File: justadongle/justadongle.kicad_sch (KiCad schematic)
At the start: 26 parts, among them U1 SL2.1A_C6798314, U2 FSUSB42MUX, U3 LMV7219M5X/NOPB, U4 HC-USB3.0-C26

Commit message: Added the footprints for all the componenets in the schematic
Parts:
- C1, C2, C3, C4, C5, C6, C7, C8, C9: footprint (none) -> Footprints:CAP-TH_BD5.0-P2.00-D0.8-FD
- D1, D2, D3, D4, D5: footprint (none) -> Footprints:SOD-323_L1.8-W1.3-LS2.5-RD
- R1, R2, R3: footprint (none) -> Footprints:RES-TH_BD2.4-L6.3-P10.30-D0.6
- U1: footprint (none) -> Footprints:SOP-16_L10.0-W3.9-P1.27-LS6.0-BL
- U2: footprint (none) -> Footprints:MSOP-10_L3.0-W3.0-P0.50-LS5.0-BL
- U3: footprint (none) -> Footprints:SOT-23-5_L3.0-W1.7-P0.95-LS2.8-BR
- U4: footprint (none) -> Footprints:USB-3.0-A-SMD_HC-USB3.0-C26
- USB2, USB3, USB4, USB5: footprint (none) -> Footprints:USB-A-TH_USB-231-ARY
- USB6: footprint (none) -> Footprints:USB-C-SMD_TYPE-C-6PIN-2MD-073
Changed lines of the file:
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@@
 			)
 		)
-		(property "Footprint" ""
+		(property "Footprint" "Footprints:SOD-323_L1.8-W1.3-LS2.5-RD"
 			(at 314.96 50.8 0)
 			(effects
@@
 			)
 		)
-		(property "Footprint" ""
+		(property "Footprint" "Footprints:USB-A-TH_USB-231-ARY"
 			(at 196.85 66.04 0)
 			(effects
@@
 			)
 		)
-		(property "Footprint" ""
+		(property "Footprint" "Footprints:USB-3.0-A-SMD_HC-USB3.0-C26"
 			(at 350.52 77.47 0)
 			(effects
@@
 			)
 		)
-		(property "Footprint" ""
+		(property "Footprint" "Footprints:SOP-16_L10.0-W3.9-P1.27-LS6.0-BL"
 			(at 90.17 55.88 0)
 			(effects
@@
 			)
 		)
-		(property "Footprint" ""
+		(property "Footprint" "Footprints:CAP-TH_BD5.0-P2.00-D0.8-FD"
 			(at 323.85 25.0952 0)
 			(effects
@@
 			)
 		)
-		(property "Footprint" ""
+		(property "Footprint" "Footprints:USB-A-TH_USB-231-ARY"
 			(at 196.85 25.4 0)
 			(effects
@@
 			)
 		)
-		(property "Footprint" ""
+		(property "Footprint" "Footprints:CAP-TH_BD5.0-P2.00-D0.8-FD"
 			(at 212.09 53.6448 0)
 			(effects
@@
 			)
 		)
-		(property "Footprint" ""
+		(property "Footprint" "Footprints:RES-TH_BD2.4-L6.3-P10.30-D0.6"
 			(at 239.522 63.5 90)
 			(effects
@@
 			)
 		)
-		(property "Footprint" ""
+		(property "Footprint" "Footprints:CAP-TH_BD5.0-P2.00-D0.8-FD"
 			(at 323.85 63.8048 0)
 			(effects
@@
 			)
 		)
-		(property "Footprint" ""
+		(property "Footprint" "Footprints:SOD-323_L1.8-W1.3-LS2.5-RD"
 			(at 314.96 39.37 0)
 			(effects
@@
 			)
 		)
-		(property "Footprint" ""
+		(property "Footprint" "Footprints:SOT-23-5_L3.0-W1.7-P0.95-LS2.8-BR"
 			(at 238.76 46.99 0)
 			(effects
@@
 			)
 		)
-		(property "Footprint" ""
+		(property "Footprint" "Footprints:USB-C-SMD_TYPE-C-6PIN-2MD-073"
 			(at 345.44 45.72 0)
 			(effects
@@
 			)
 		)
-		(property "Footprint" ""
+		(property "Footprint" "Footprints:SOD-323_L1.8-W1.3-LS2.5-RD"
 			(at 332.74 87.63 0)
 			(effects
@@
 			)
 		)
-		(property "Footprint" ""
+		(property "Footprint" "Footprints:CAP-TH_BD5.0-P2.00-D0.8-FD"
 			(at 213.36 97.4852 0)
 			(effects
@@
 			)
 		)
-		(property "Footprint" ""
+		(property "Footprint" "Footprints:CAP-TH_BD5.0-P2.00-D0.8-FD"
 			(at 336.55 94.2848 0)
 			(effects
@@
 			)
 		)
-		(property "Footprint" ""
+		(property "Footprint" "Footprints:CAP-TH_BD5.0-P2.00-D0.8-FD"
 			(at 126.6952 45.72 0)
 			(effects
@@
 			)
 		)
-		(property "Footprint" ""
+		(property "Footprint" "Footprints:CAP-TH_BD5.0-P2.00-D0.8-FD"
 			(at 139.3952 45.72 0)
 			(effects
@@
 			)
 		)
-		(property "Footprint" ""
+		(property "Footprint" "Footprints:SOD-323_L1.8-W1.3-LS2.5-RD"
 			(at 328.93 34.29 0)
 			(effects
@@
 			)
 		)
-		(property "Footprint" ""
+		(property "Footprint" "Footprints:USB-A-TH_USB-231-ARY"
 			(at 196.85 86.36 0)
 			(effects
@@
 			)
 		)
-		(property "Footprint" ""
+		(property "Footprint" "Footprints:SOD-323_L1.8-W1.3-LS2.5-RD"
 			(at 325.12 57.15 0)
 			(effects
@@
 			)
 		)
-		(property "Footprint" ""
+		(property "Footprint" "Footprints:RES-TH_BD2.4-L6.3-P10.30-D0.6"
 			(at 247.65 32.258 90)
 			(effects
@@
 			)
 		)
-		(property "Footprint" ""
+		(property "Footprint" "Footprints:CAP-TH_BD5.0-P2.00-D0.8-FD"
 			(at 212.09 33.3248 0)
 			(effects
@@
 			)
 		)
-		(property "Footprint" ""
+		(property "Footprint" "Footprints:CAP-TH_BD5.0-P2.00-D0.8-FD"
 			(at 212.09 73.9648 0)
 			(effects
@@
 			)
 		)
-		(property "Footprint" ""
+		(property "Footprint" "Footprints:RES-TH_BD2.4-L6.3-P10.30-D0.6"
 			(at 245.618 22.86 90)
 			(effects
@@
 			)
 		)
-		(property "Footprint" ""
+		(property "Footprint" "Footprints:MSOP-10_L3.0-W3.0-P0.50-LS5.0-BL"
 			(at 283.21 55.88 0)
 			(effects
@@
 			)
 		)
-		(property "Footprint" ""
+		(property "Footprint" "Footprints:USB-A-TH_USB-231-ARY"
 			(at 196.85 45.72 0)
 			(effects

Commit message: Finished the Board
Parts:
- added C10, C11: 15pf, Footprints:CAP-TH_BD5.0-P2.00-D0.8-FD, symbol Device:C
- added Y1: 12Mhz, easyeda2kicad:CRYSTAL-SMD_4P-L3.2-W2.5-BL, symbol Device:Crystal
- C1, C2, C3, C4, C5, C6, C7, C8, C9: footprint Footprints:CAP-TH_BD5.0-P2.00-D0.8-FD -> easyeda2kicad:C0805
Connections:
- net GND: now also C10.1, C11.1; no longer U1.16 (XIN)
- net at U1.15 (XOUT): now also C11.2, Y1.2
- new net: C10.2, U1.16 (XIN), Y1.1
- no-connect marks 10 -> 9
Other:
- moved on the sheet: C1, C8, C9, D1, D2, D3, D4, D5, U2, U4, USB6

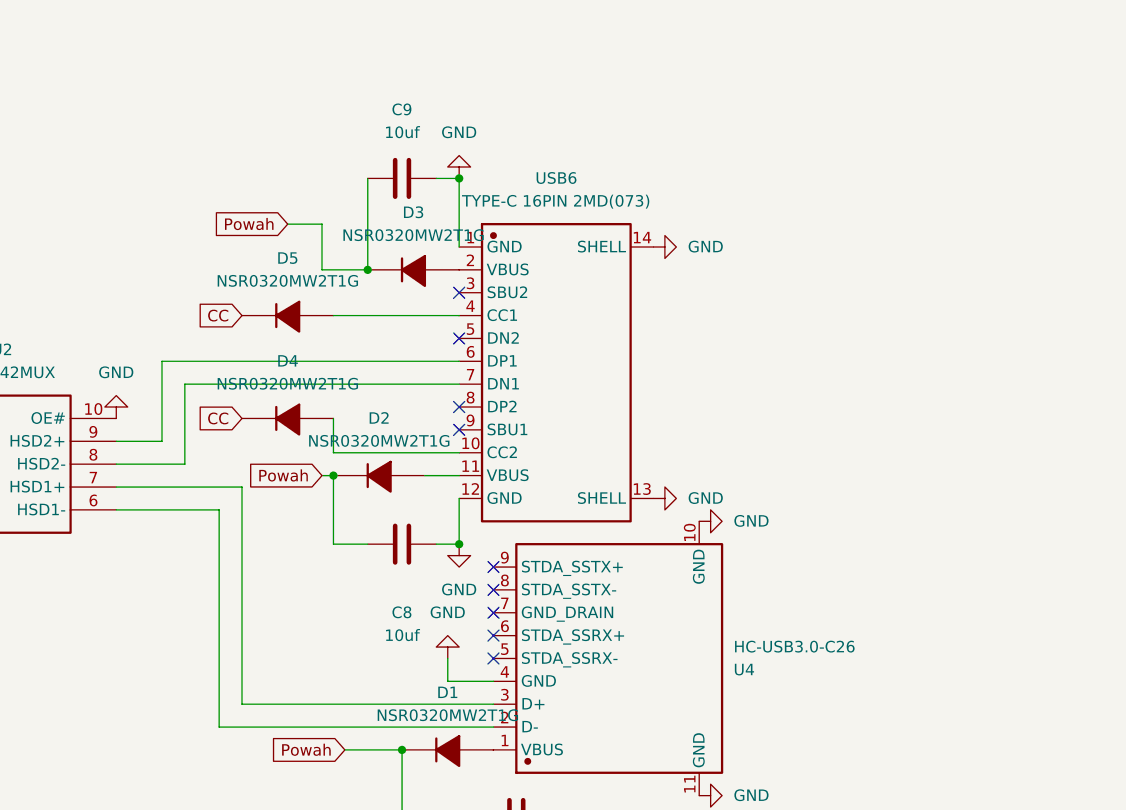
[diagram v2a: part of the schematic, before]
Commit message: corrected the usb -c symbol and wired it
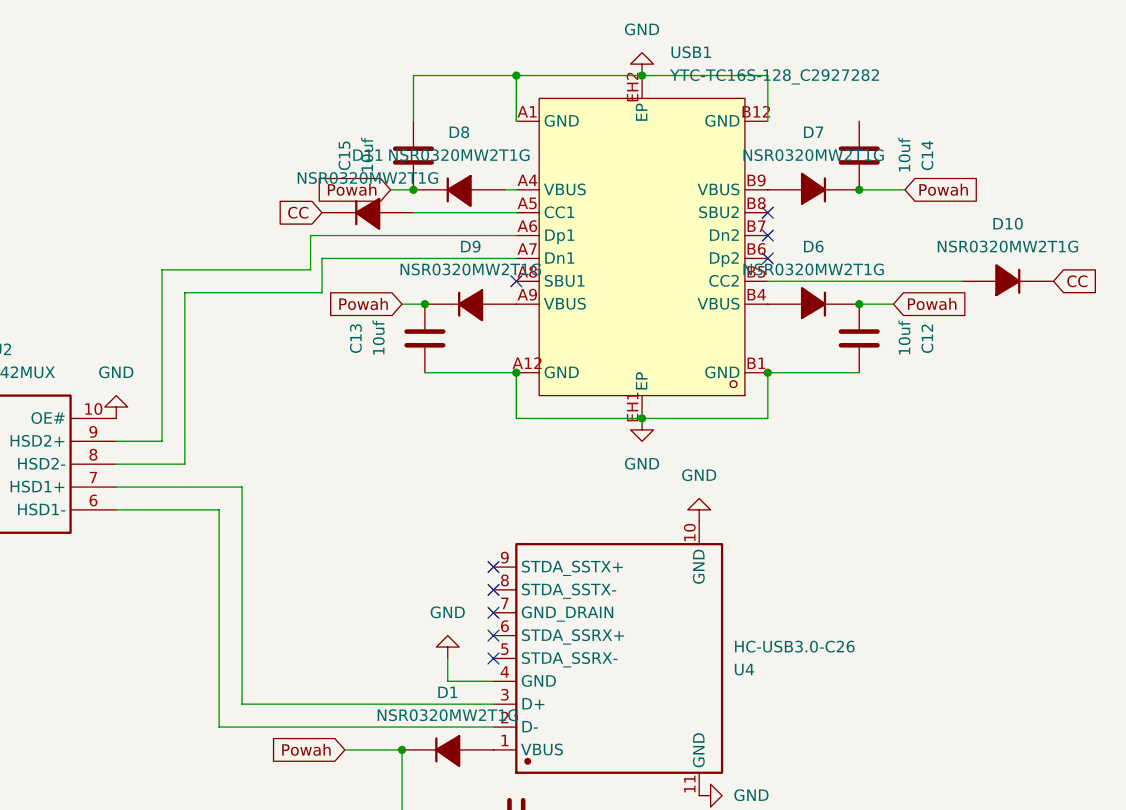
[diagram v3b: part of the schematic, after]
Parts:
- removed C8, C9: 10uf, easyeda2kicad:C0805, symbol Device:C
- removed D2, D3, D4, D5: NSR0320MW2T1G, Footprints:SOD-323_L1.8-W1.3-LS2.5-RD, symbol SCHLIB_NSR0320MW2T1G_2025-08-14:NSR0320MW2T1G
- removed USB6: TYPE-C 16PIN 2MD(073), Footprints:USB-C-SMD_TYPE-C-6PIN-2MD-073, symbol SCHLIB_TYPE-C-16PIN-2MD(073)_2025-08-14 (1):TYPE-C 16PIN 2MD(073)
- added C12, C13, C14, C15: 10uf, easyeda2kicad:C0805, symbol Device:C
- added D10, D11, D6, D7, D8, D9: NSR0320MW2T1G, Footprints:SOD-323_L1.8-W1.3-LS2.5-RD, symbol SCHLIB_NSR0320MW2T1G_2025-08-14:NSR0320MW2T1G
- added USB1: YTC-TC16S-128_C2927282, easyeda2kicad:TYPE-C-SMD_YTC-TC16S-128, symbol easyeda2kicad:YTC-TC16S-128_C2927282
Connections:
- net CC: now also D10.1 (C), D11.1 (C)
- net GND: now also C12.2, C13.1, C15.2, USB1.A1 (GND), USB1.A12 (GND), USB1.B1 (GND), USB1.B12 (GND), USB1.EH1 (EP), USB1.EH2 (EP)
- net Powah: now also C12.1, C13.2, C14.2, C15.1, D6.1 (C), D7.1 (C), D8.1 (C), D9.1 (C)
- net at U2.9 (HSD2+): now also USB1.A6 (Dp1)
- net at U2.8 (HSD2-): now also USB1.A7 (Dn1)
- new net: D9.2 (A), USB1.A9 (VBUS)
- new net: D11.2 (A), USB1.A5 (CC1)
- new net: D10.2 (A), USB1.B5 (CC2)
- new net: D7.2 (A), USB1.B9 (VBUS)
- new net: D8.2 (A), USB1.A4 (VBUS)
- new net: D6.2 (A), USB1.B4 (VBUS)

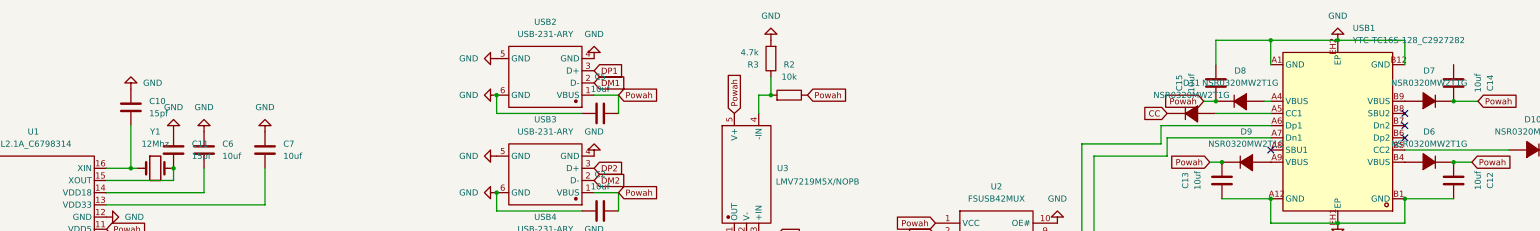
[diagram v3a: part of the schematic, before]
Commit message: redesigned the whole thingy cause of the messed up c port and additional capacitors and diodes
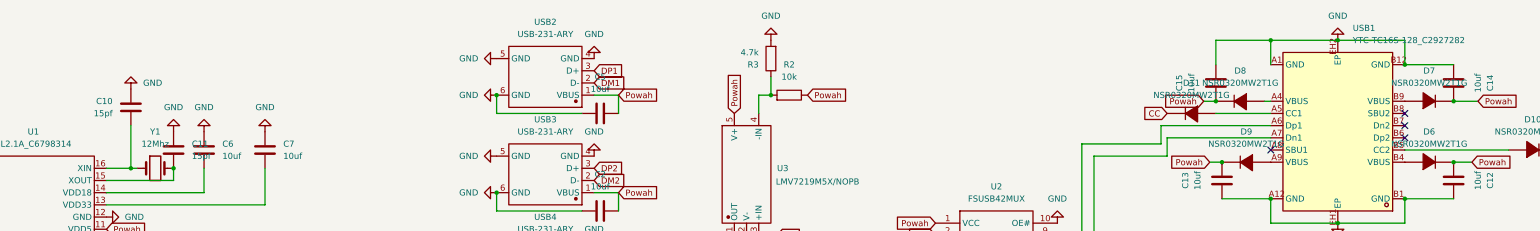
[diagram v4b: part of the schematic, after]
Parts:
- C1, C12, C13, C14, C15, C2, C3, C4, C5, C6, C7: footprint easyeda2kicad:C0805 -> Footprints:C0805
- USB1: footprint easyeda2kicad:TYPE-C-SMD_YTC-TC16S-128 -> Footprints:TYPE-C-SMD_YTC-TC16S-128
- Y1: footprint easyeda2kicad:CRYSTAL-SMD_4P-L3.2-W2.5-BL -> Footprints:CAP-TH_BD5.0-P2.00-D0.8-FD
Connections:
- net GND: now also C14.1
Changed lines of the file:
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@@
 	)
 	(junction
+		(at 375.92 24.13)
+		(diameter 0)
+		(color 0 0 0 0)
+	)
+	(junction
 		(at 347.98 52.07)
 		(diameter 0)
@@
 	(wire
 		(pts
+			(xy 386.08 24.13) (xy 375.92 24.13)
+		)
+		(stroke
+			(width 0)
+			(type default)
+		)
+	)
+	(wire
+		(pts
 			(xy 337.82 52.07) (xy 347.98 52.07)
 		)
@@
 	(wire
 		(pts
-			(xy 375.92 24.13) (xy 375.92 19.05)
+			(xy 375.92 19.05) (xy 375.92 24.13)
 		)
 		(stroke
@@
 			)
 		)
-		(property "Footprint" "easyeda2kicad:C0805"
+		(property "Footprint" "Footprints:C0805"
 			(at 338.7852 44.45 0)
 			(effects
@@
 			)
 		)
-		(property "Footprint" "easyeda2kicad:CRYSTAL-SMD_4P-L3.2-W2.5-BL"
+		(property "Footprint" "Footprints:CAP-TH_BD5.0-P2.00-D0.8-FD"
 			(at 115.57 45.72 0)
 			(effects
@@
 			)
 		)
-		(property "Footprint" "easyeda2kicad:C0805"
+		(property "Footprint" "Footprints:C0805"
 			(at 212.09 53.6448 0)
 			(effects
@@
 		(lib_id "Device:C")
 		(at 110.49 33.02 0)
+		(mirror y)
 		(unit 1)
 		(exclude_from_sim no)
@@
 		(on_board yes)
 		(dnp no)
-		(fields_autoplaced yes)
 		(property "Reference" "C10"
-			(at 114.3 31.7499 0)
+			(at 106.68 31.7499 0)
 			(effects
 				(font
@@
 		)
 		(property "Value" "15pf"
-			(at 114.3 34.2899 0)
+			(at 106.68 34.2899 0)
 			(effects
 				(font
@@
 		)
 		(property "Footprint" "Footprints:CAP-TH_BD5.0-P2.00-D0.8-FD"
-			(at 111.4552 36.83 0)
+			(at 109.5248 36.83 0)
 			(effects
 				(font
@@
 			)
 		)
-		(property "Footprint" "easyeda2kicad:C0805"
+		(property "Footprint" "Footprints:C0805"
 			(at 385.1148 52.07 0)
 			(effects
@@
 			)
 		)
-		(property "Footprint" "easyeda2kicad:C0805"
+		(property "Footprint" "Footprints:C0805"
 			(at 213.36 97.4852 0)
 			(effects
@@
 			)
 		)
-		(property "Footprint" "easyeda2kicad:C0805"
+		(property "Footprint" "Footprints:C0805"
 			(at 344.17 100.6348 0)
 			(effects
@@
 			)
 		)
-		(property "Footprint" "easyeda2kicad:C0805"
+		(property "Footprint" "Footprints:C0805"
 			(at 126.6952 45.72 0)
 			(effects
@@
 			)
 		)
-		(property "Footprint" "easyeda2kicad:C0805"
+		(property "Footprint" "Footprints:C0805"
 			(at 139.3952 45.72 0)
 			(effects
@@
 			)
 		)
-		(property "Footprint" "easyeda2kicad:C0805"
+		(property "Footprint" "Footprints:C0805"
 			(at 212.09 33.3248 0)
 			(effects
@@
 			)
 		)
-		(property "Footprint" "easyeda2kicad:C0805"
+		(property "Footprint" "Footprints:C0805"
 			(at 212.09 73.9648 0)
 			(effects
@@
 			)
 		)
-		(property "Footprint" "easyeda2kicad:C0805"
+		(property "Footprint" "Footprints:C0805"
 			(at 385.1148 31.75 0)
 			(effects
@@
 			)
 		)
-		(property "Footprint" "easyeda2kicad:C0805"
+		(property "Footprint" "Footprints:C0805"
 			(at 337.5152 24.13 0)
 			(effects
@@
 			)
 		)
-		(property "Footprint" "easyeda2kicad:TYPE-C-SMD_YTC-TC16S-128"
+		(property "Footprint" "Footprints:TYPE-C-SMD_YTC-TC16S-128"
 			(at 361.95 11.43 0)
 			(effects
